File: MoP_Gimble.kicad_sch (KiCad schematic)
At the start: 16 parts, among them J401 Conn_01x02, J402 282837-2, J403 282837-2, J404 Camera, J405 Conn_01x02, J405 Steering, U401 L293D, U402 74LVC2G14

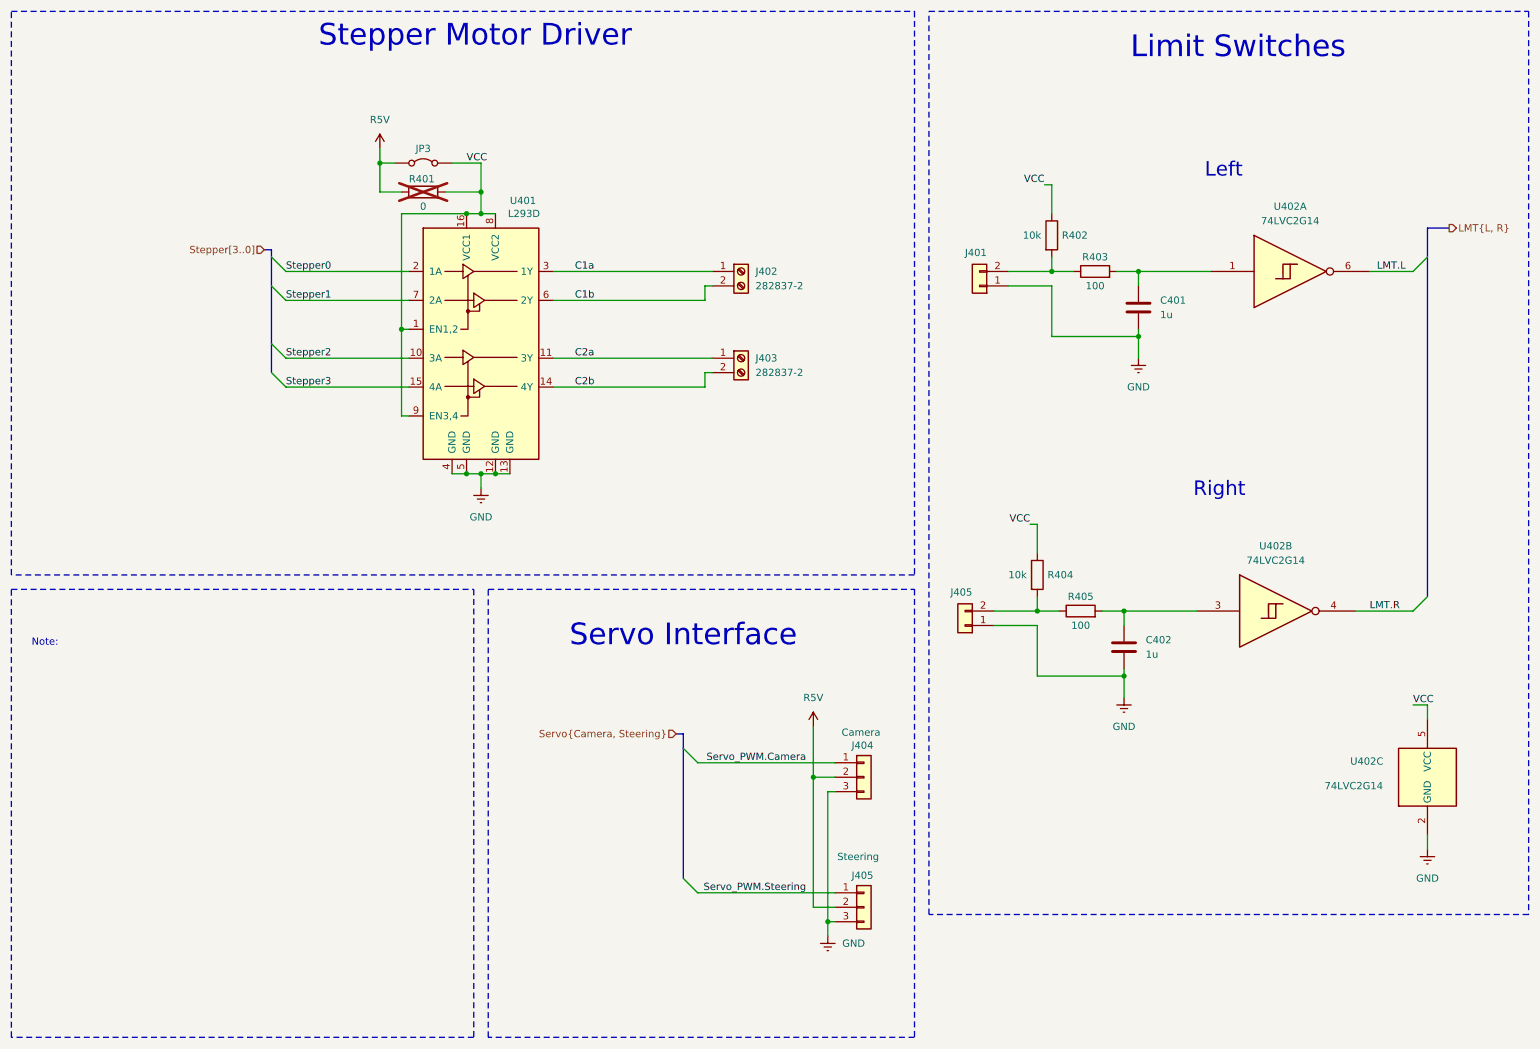
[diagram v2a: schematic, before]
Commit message: Added subproject for EPS PCB
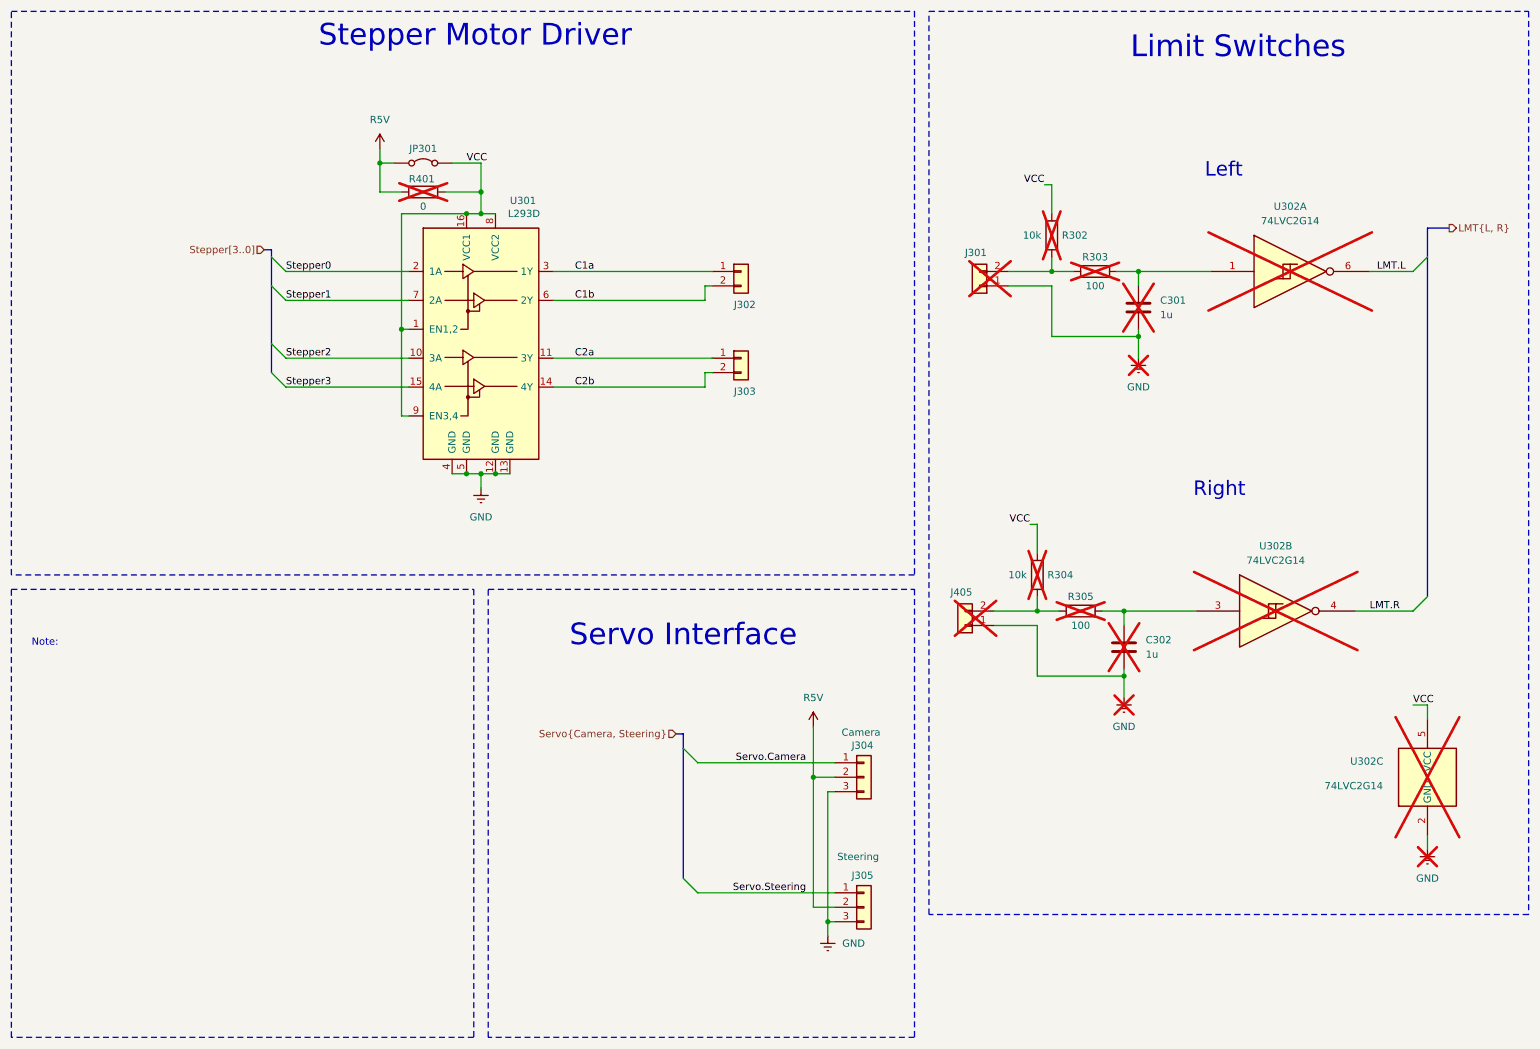
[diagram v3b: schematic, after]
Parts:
- removed J402, J403: 282837-2, TerminalBlock_Phoenix:TerminalBlock_Phoenix_MKDS-1,5-2-5.08_1x02_P5.08mm_Horizontal, symbol Connector:Screw_Terminal_01x02
- added J302, J303: Conn_01x02, Connector_PinHeader_2.54mm:PinHeader_1x02_P2.54mm_Vertical, symbol Connector_Generic:Conn_01x02
- C301: renamed from C401; footprint (none) -> Capacitor_SMD:C_0805_2012Metric; now not fitted
- C302: renamed from C402; now not fitted
- J301: renamed from J401; footprint (none) -> Connector_PinHeader_2.54mm:PinHeader_1x02_P2.54mm_Vertical; now not fitted
- J304: renamed from J404; footprint Connector_PinHeader_2.54mm:PinHeader_1x02_P2.54mm_Vertical -> Connector_PinHeader_2.54mm:PinHeader_1x03_P2.54mm_Vertical
- J305: renamed from J405; footprint (none) -> Connector_PinHeader_2.54mm:PinHeader_1x03_P2.54mm_Vertical
- J405: footprint (none) -> Connector_PinHeader_2.54mm:PinHeader_1x02_P2.54mm_Vertical; now not fitted
- R302: renamed from R402; now not fitted
- R303: renamed from R403; now not fitted
- R304: renamed from R404; now not fitted
- R305: renamed from R405; now not fitted
- U302: renamed from U402; now not fitted
- renumbered JP3 to JP301, U401 to U301
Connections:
- net C1a: now also J302.1 (Pin_1)
- net C1b: now also J302.2 (Pin_2)
- net C2a: now also J303.1 (Pin_1)
- net C2b: now also J303.2 (Pin_2)
- net Servo_PWM.Camera renamed Servo.Camera
- net Servo_PWM.Steering renamed Servo.Steering

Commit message: added OBC
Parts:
- C301, C302, J301, J405, R302, R303, R304, R305, U302: now fitted
- J302, J303, U301: now not fitted
- J304, J305: now not fitted; now left out of the parts list
